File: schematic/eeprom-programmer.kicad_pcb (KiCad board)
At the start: 2 copper layers, 8 parts, among them IC1 AT28C64B-15PU, U1 74HC595, U2 74HC595

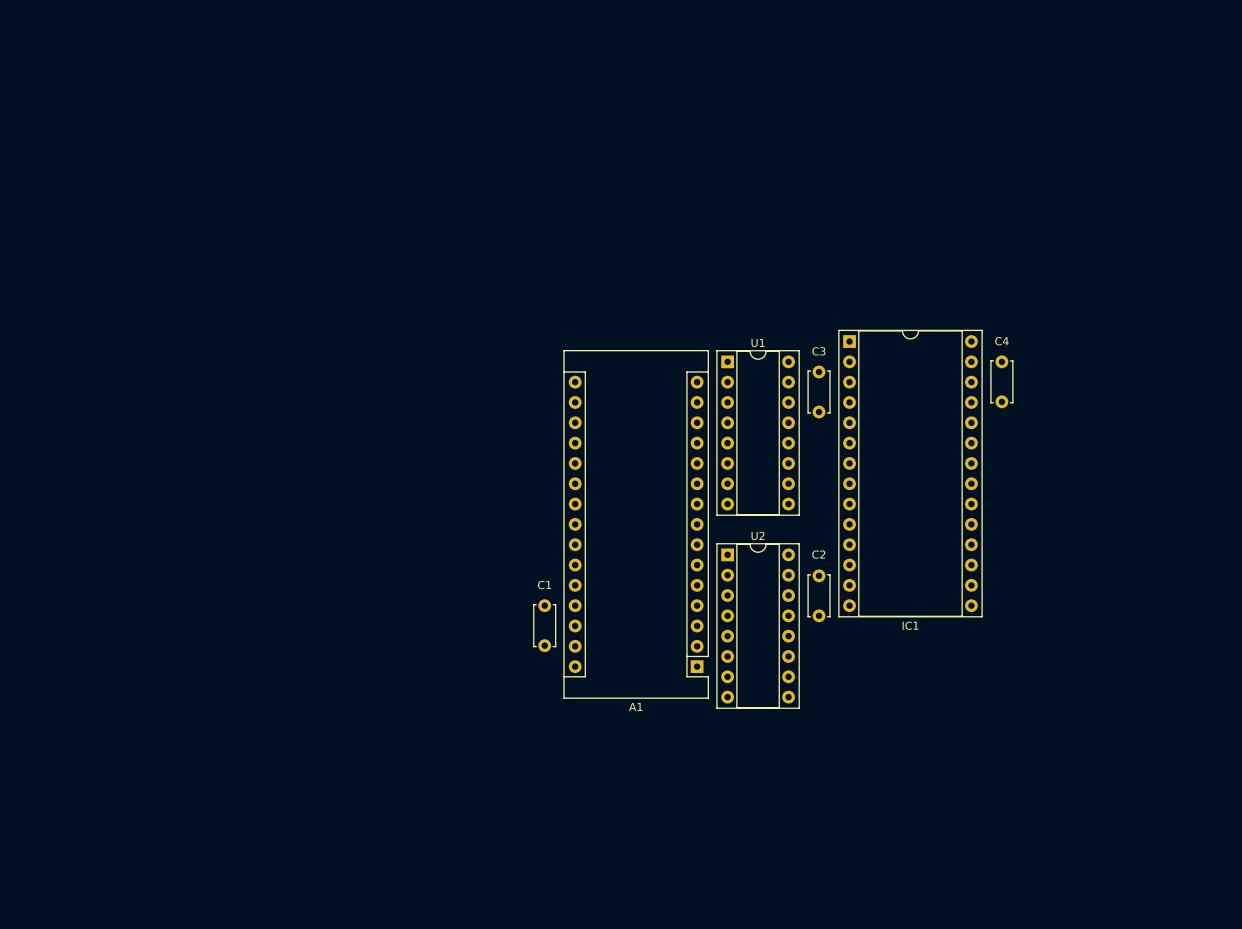
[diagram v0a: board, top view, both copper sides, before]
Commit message: Initial PCB routing
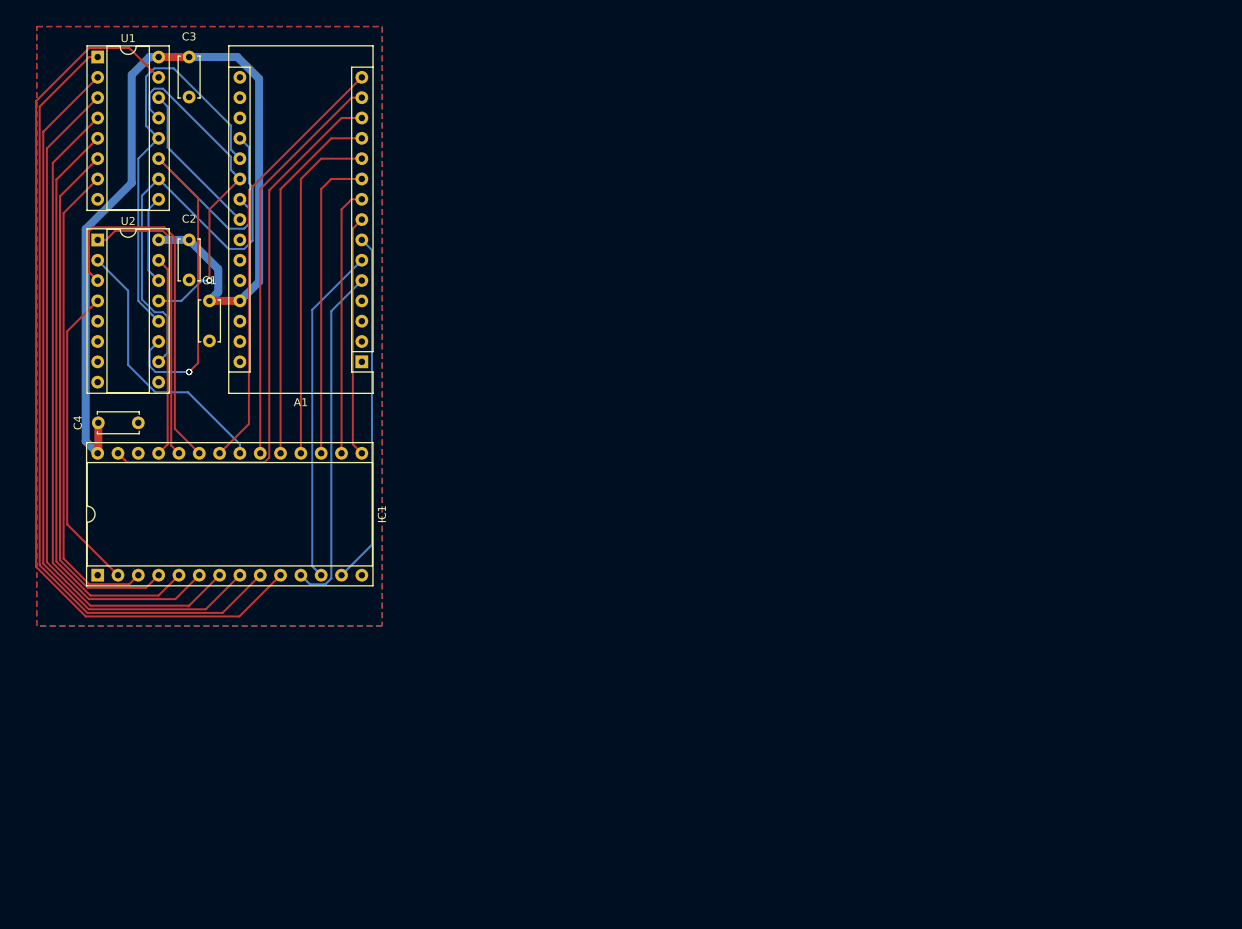
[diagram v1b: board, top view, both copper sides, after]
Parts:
- moved C4 108.0 mm to (36.8, 74.9), turned to 180 degrees
- moved IC1 98.4 mm to (31.8, 94.0), turned to 90 degrees
- moved C2 89.2 mm to (43.2, 52.1)
- moved C3 88.0 mm to (43.2, 29.2)
- moved U2 88.0 mm to (31.8, 52.1)
- moved U1 87.5 mm to (31.8, 29.2)
- moved A1 56.6 mm to (64.8, 67.3)
- moved C1 56.6 mm to (45.7, 59.7)
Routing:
- net Arduino5V: track 0.00 -> 118.1 mm
- net /addr00: track 0.00 -> 113.1 mm
- net /addr01: track 0.00 -> 99.1 mm
- net /addr02: track 0.00 -> 92.3 mm
- net /addr03: track 0.00 -> 86.1 mm
- net /addr04: track 0.00 -> 79.4 mm
- net /addr05: track 0.00 -> 73.2 mm
- net eeNotWriteEnable: track 0.00 -> 68.3 mm
- net /addr06: track 0.00 -> 66.5 mm
- net /addr07: track 0.00 -> 60.4 mm
- net srSerialClock: track 0.00 -> 56.7 mm, vias 0 -> 2
- net srNotResetAll: track 0.00 -> 55.4 mm
- net eeNotOutputEnable: track 0.00 -> 54.4 mm
- net srReadClock: track 0.00 -> 51.9 mm
- net eeNotChipEnable: track 0.00 -> 50.5 mm
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- added copper zone on B.Cu, net GND
- added copper zone on F.Cu, net GND

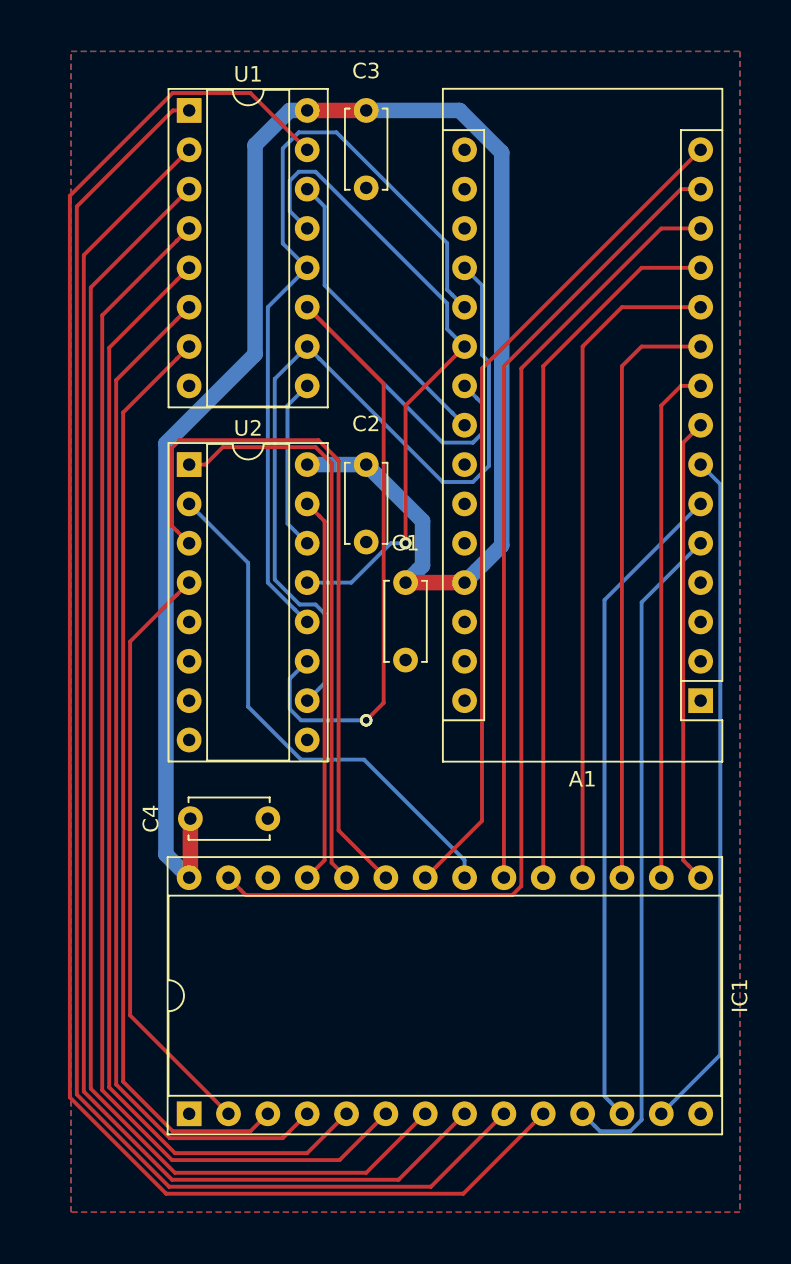
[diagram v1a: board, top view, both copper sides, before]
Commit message: Fix issues for OSHPARK submission
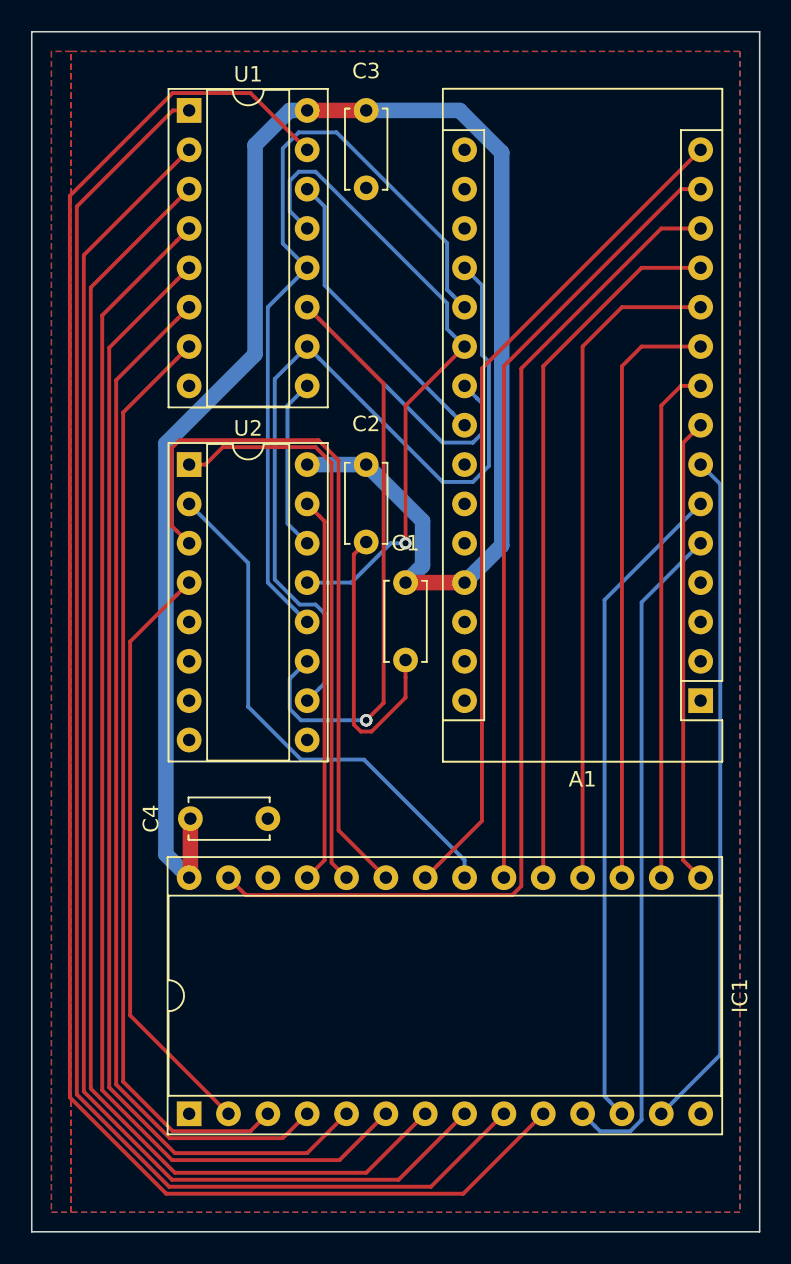
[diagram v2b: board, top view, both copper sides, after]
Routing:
- net GND: track 0.00 -> 19.0 mm
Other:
- board outline added: 47 x 77.5 mm
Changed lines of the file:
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@@
   (general
     (thickness 1.6)
-    (drawings 0)
-    (tracks 208)
+    (drawings 4)
+    (tracks 215)
     (zones 0)
     (modules 8)
@@
     )
   )
+  (gr_line (start 21.59 101.6) (end 21.59 24.13) (layer Edge.Cuts) (width 0.1))
+  (gr_line (start 68.58 101.6) (end 21.59 101.6) (layer Edge.Cuts) (width 0.1))
+  (gr_line (start 68.58 24.13) (end 68.58 101.6) (layer Edge.Cuts) (width 0.1))
+  (gr_line (start 21.59 24.13) (end 68.58 24.13) (layer Edge.Cuts) (width 0.1))
   (segment (start 48.115001 53.195001) (end 40.169999 45.249999) (width 0.25) (layer B.Cu) (net 1))
   (segment (start 40.169999 45.249999) (end 39.37 44.45) (width 0.25) (layer B.Cu) (net 1))
@@
   (segment (start 53.195001 45.864999) (end 53.195001 79.280001) (width 0.25) (layer F.Cu) (net 15))
   (segment (start 62.23 36.83) (end 53.195001 45.864999) (width 0.25) (layer F.Cu) (net 15))
+  (segment (start 45.72 67.113002) (end 45.72 65.82137) (width 0.25) (layer F.Cu) (net 16))
+  (segment (start 43.528001 69.305001) (end 45.72 67.113002) (width 0.25) (layer F.Cu) (net 16))
+  (segment (start 45.72 65.82137) (end 45.72 64.69) (width 0.25) (layer F.Cu) (net 16))
+  (segment (start 42.380001 68.853003) (end 42.831999 69.305001) (width 0.25) (layer F.Cu) (net 16))
+  (segment (start 42.831999 69.305001) (end 43.528001 69.305001) (width 0.25) (layer F.Cu) (net 16))
+  (segment (start 42.380001 57.869999) (end 42.380001 68.853003) (width 0.25) (layer F.Cu) (net 16))
+  (segment (start 43.18 57.07) (end 42.380001 57.869999) (width 0.25) (layer F.Cu) (net 16))
   (segment (start 64.77 34.29) (end 63.5 34.29) (width 0.25) (layer F.Cu) (net 17))
   (segment (start 63.5 34.29) (end 52.07 45.72) (width 0.25) (layer F.Cu) (net 17))
@@
       )
     )
+  )
+  (zone (net 16) (net_name GND) (layer F.Cu) (hatch edge 0.508)
+    (connect_pads (clearance 0.508))
+    (min_thickness 0.254)
+    (fill yes (arc_segments 32) (thermal_gap 0.508) (thermal_bridge_width 0.508))
+    (polygon
+      (pts
+        (xy 24.13 25.4) (xy 22.86 25.4) (xy 22.86 100.33) (xy 24.13 100.33)
+      )
+    )
+  )
+  (zone (net 16) (net_name GND) (layer B.Cu) (hatch edge 0.508)
+    (connect_pads (clearance 0.508))
+    (min_thickness 0.254)
+    (fill yes (arc_segments 32) (thermal_gap 0.508) (thermal_bridge_width 0.508))
+    (polygon
+      (pts
+        (xy 22.86 25.4) (xy 22.86 100.33) (xy 24.13 100.33) (xy 24.13 25.4)
+      )
+    )

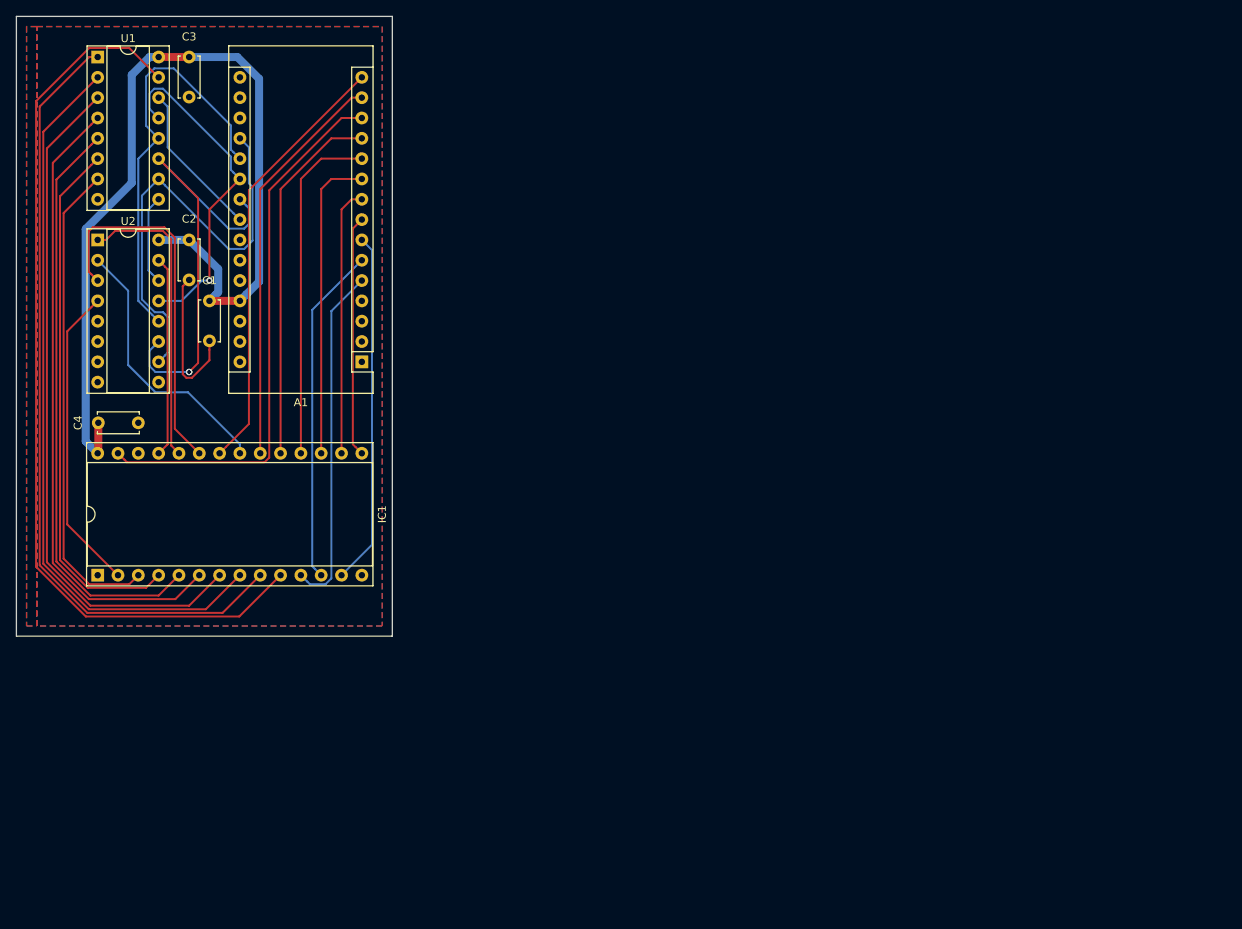
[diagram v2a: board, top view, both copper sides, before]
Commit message: Begin new layout using better design limits
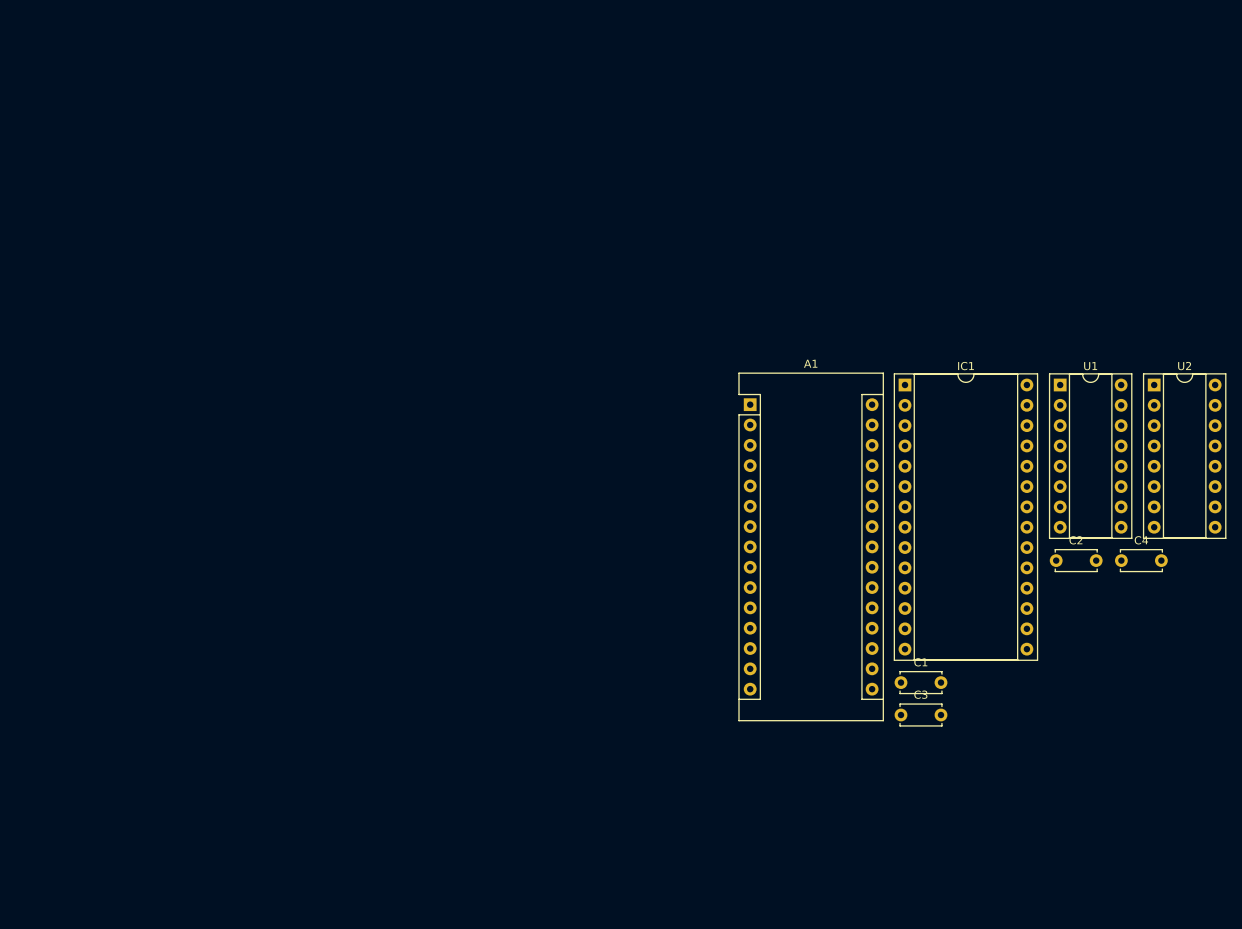
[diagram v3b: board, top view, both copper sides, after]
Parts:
- moved U2 133.3 mm to (163.8, 70.2)
- moved U1 127.1 mm to (152.1, 70.2)
- moved C4 124.1 mm to (159.7, 92.2), turned to 0 degrees
- moved C3 121.2 mm to (132.2, 111.5), turned to 0 degrees
- moved C2 115.6 mm to (151.6, 92.2), turned to 0 degrees
- moved IC1 103.7 mm to (132.7, 70.2), turned to 0 degrees
- moved C1 98.7 mm to (132.2, 107.4), turned to 0 degrees
- moved A1 48.8 mm to (113.3, 72.7), turned to 0 degrees
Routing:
- net Arduino5V: track 118.1 -> 0.00 mm
- net /addr00: track 113.1 -> 0.00 mm
- net /addr01: track 99.1 -> 0.00 mm
- net /addr02: track 92.3 -> 0.00 mm
- net /addr03: track 86.1 -> 0.00 mm
- net /addr04: track 79.4 -> 0.00 mm
- net /addr05: track 73.2 -> 0.00 mm
- net eeNotWriteEnable: track 68.3 -> 0.00 mm
- net /addr06: track 66.5 -> 0.00 mm
- net /addr07: track 60.4 -> 0.00 mm
- net srSerialClock: track 56.7 -> 0.00 mm, vias 2 -> 0
- net srNotResetAll: track 55.4 -> 0.00 mm
- net eeNotOutputEnable: track 54.4 -> 0.00 mm
- net srReadClock: track 51.9 -> 0.00 mm
- net eeNotChipEnable: track 50.5 -> 0.00 mm
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- removed copper zone on B.Cu, net GND
- removed copper zone on F.Cu, net GND
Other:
- board outline removed
- net class Default: clearance 0.2 -> 0.1524; trace_width 0.25 -> 0.1534; via_dia 0.8 -> 0.508; via_drill 0.4 -> 0.254
- rule trace_clearance: 0.2 -> 0.1524
- rule trace_min: 0.2 -> 0.1524
- rule via_min_drill: 0.3 -> 0.254
- rule via_min_size: 0.4 -> 0.508

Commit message: Rearrange parts
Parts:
- moved IC1 73.4 mm to (95.2, 133.3), turned to 90 degrees
- moved U2 72.2 mm to (95.2, 92.7)
- moved C4 68.1 mm to (95.3, 114.3)
- moved U1 56.8 mm to (95.2, 69.8)
- moved C2 44.7 mm to (108.0, 82.5), turned to 270 degrees
- moved A1 38.3 mm to (128.3, 108.0), turned to 180 degrees
- moved C1 27.7 mm to (108.0, 94.0), turned to 270 degrees
- moved C3 25.0 mm to (108.0, 105.4), turned to 270 degrees

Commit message: Add routing
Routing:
- net /addr02: track 0.00 -> 85.1 mm
- net /addr01: track 0.00 -> 84.7 mm
- net eeNotWriteEnable: track 0.00 -> 79.2 mm
- net /addr00: track 0.00 -> 70.5 mm, vias 0 -> 3
- net Arduino5V: track 0.00 -> 67.6 mm
- net /addr03: track 0.00 -> 65.0 mm, vias 0 -> 2
- net /addr04: track 0.00 -> 61.1 mm, vias 0 -> 2
- net eeNotOutputEnable: track 0.00 -> 58.1 mm
- net /addr05: track 0.00 -> 57.5 mm, vias 0 -> 2
- net /addr06: track 0.00 -> 54.5 mm, vias 0 -> 2
- net eeNotChipEnable: track 0.00 -> 50.7 mm
- net /addr07: track 0.00 -> 50.6 mm, vias 0 -> 2
- net /data0: track 0.00 -> 44.8 mm
- net /data1: track 0.00 -> 43.5 mm
- net /data7: track 0.00 -> 43.4 mm
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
